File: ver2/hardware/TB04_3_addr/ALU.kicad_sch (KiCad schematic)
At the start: 8 parts, among them J801 Conn_02x05_Odd_Even, J802 Conn_02x05_Odd_Even, J803 Conn_02x05_Odd_Even, J804 Conn_02x05_Odd_Even, J805 Conn_02x05_Odd_Even, J806 Conn_02x05_Odd_Even, J807 Conn_02x05_Odd_Even, J808 Conn_02x05_Odd_Even

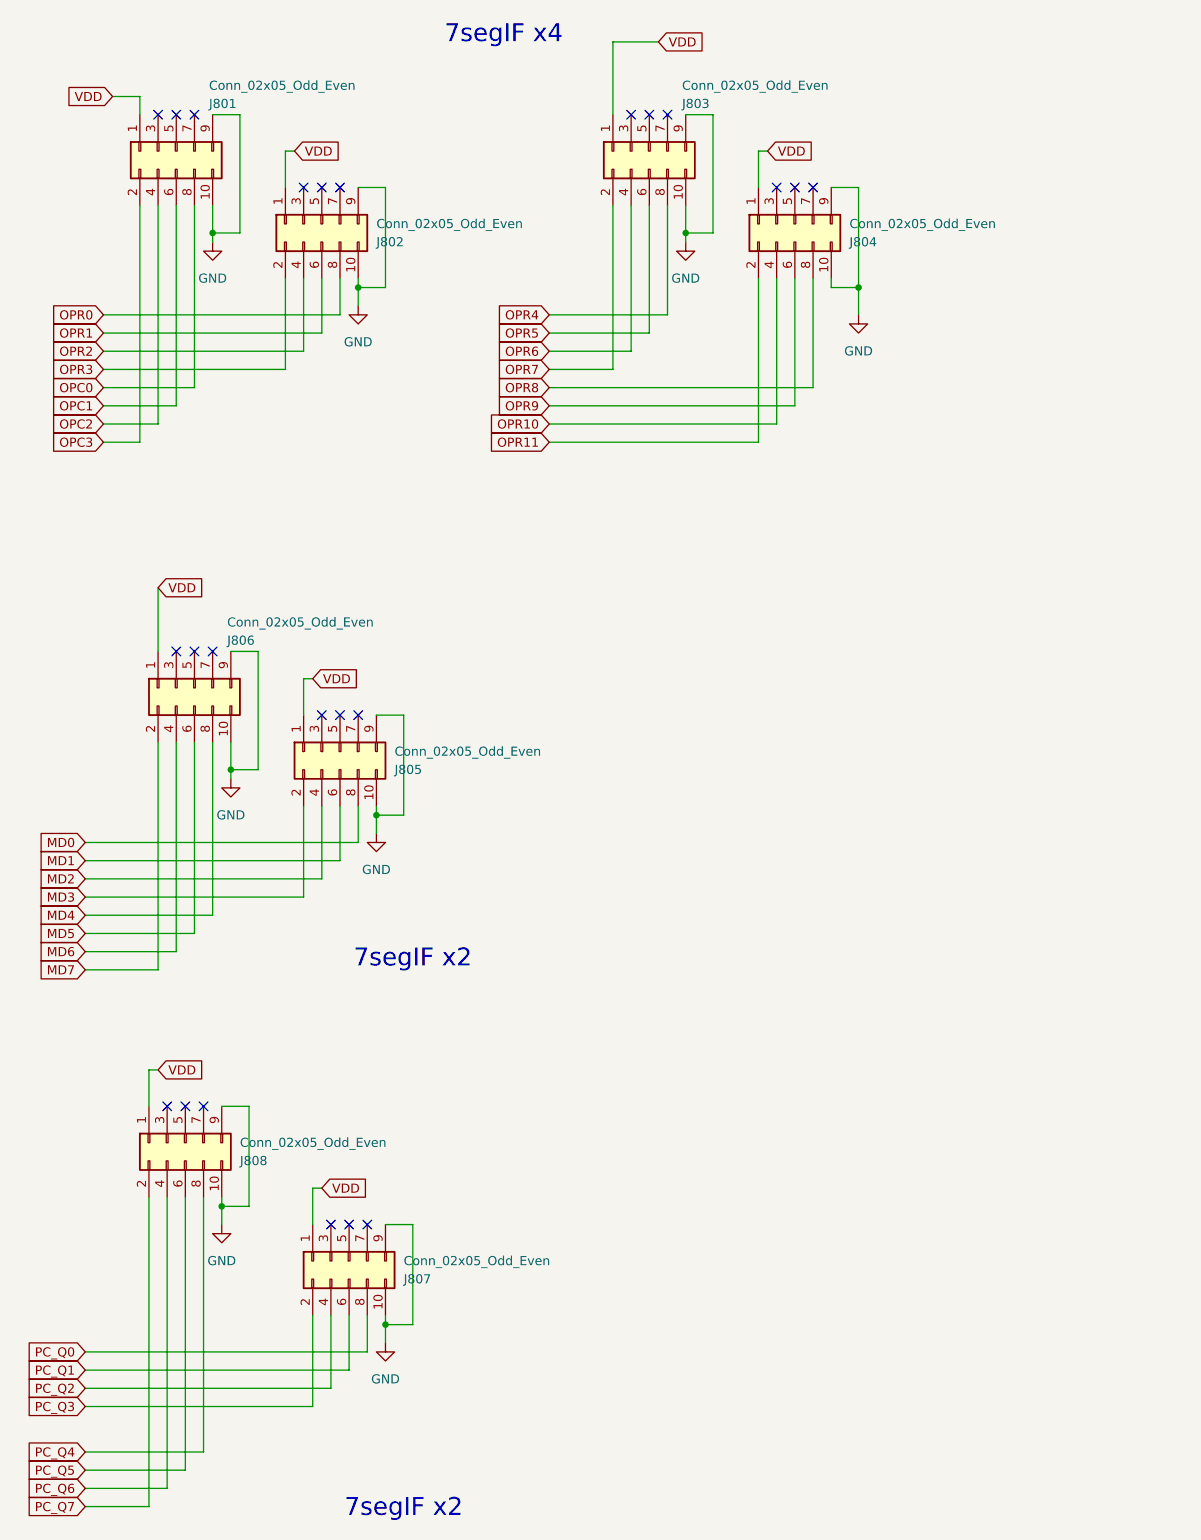
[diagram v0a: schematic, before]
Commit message: ver2: アドレス基板を分割し4枚すべて完了(要修正1件)
TB04_3_addr を分割。45部品・56信号すべてバスへ引き出し済み。
署名が変わったのは J101 のみ(USB-C→バスヘッダ)。
旧トップシート TB04addr8bit.kicad_sch も削除。

要修正: 3_addr の J103 で INPUT/OUTPUT のビット順が 4_io と逆
(pin25=INPUT0 になっている。正は pin25=INPUT3)

Co-Authored-By: Claude Opus 5 <noreply@anthropic.com>
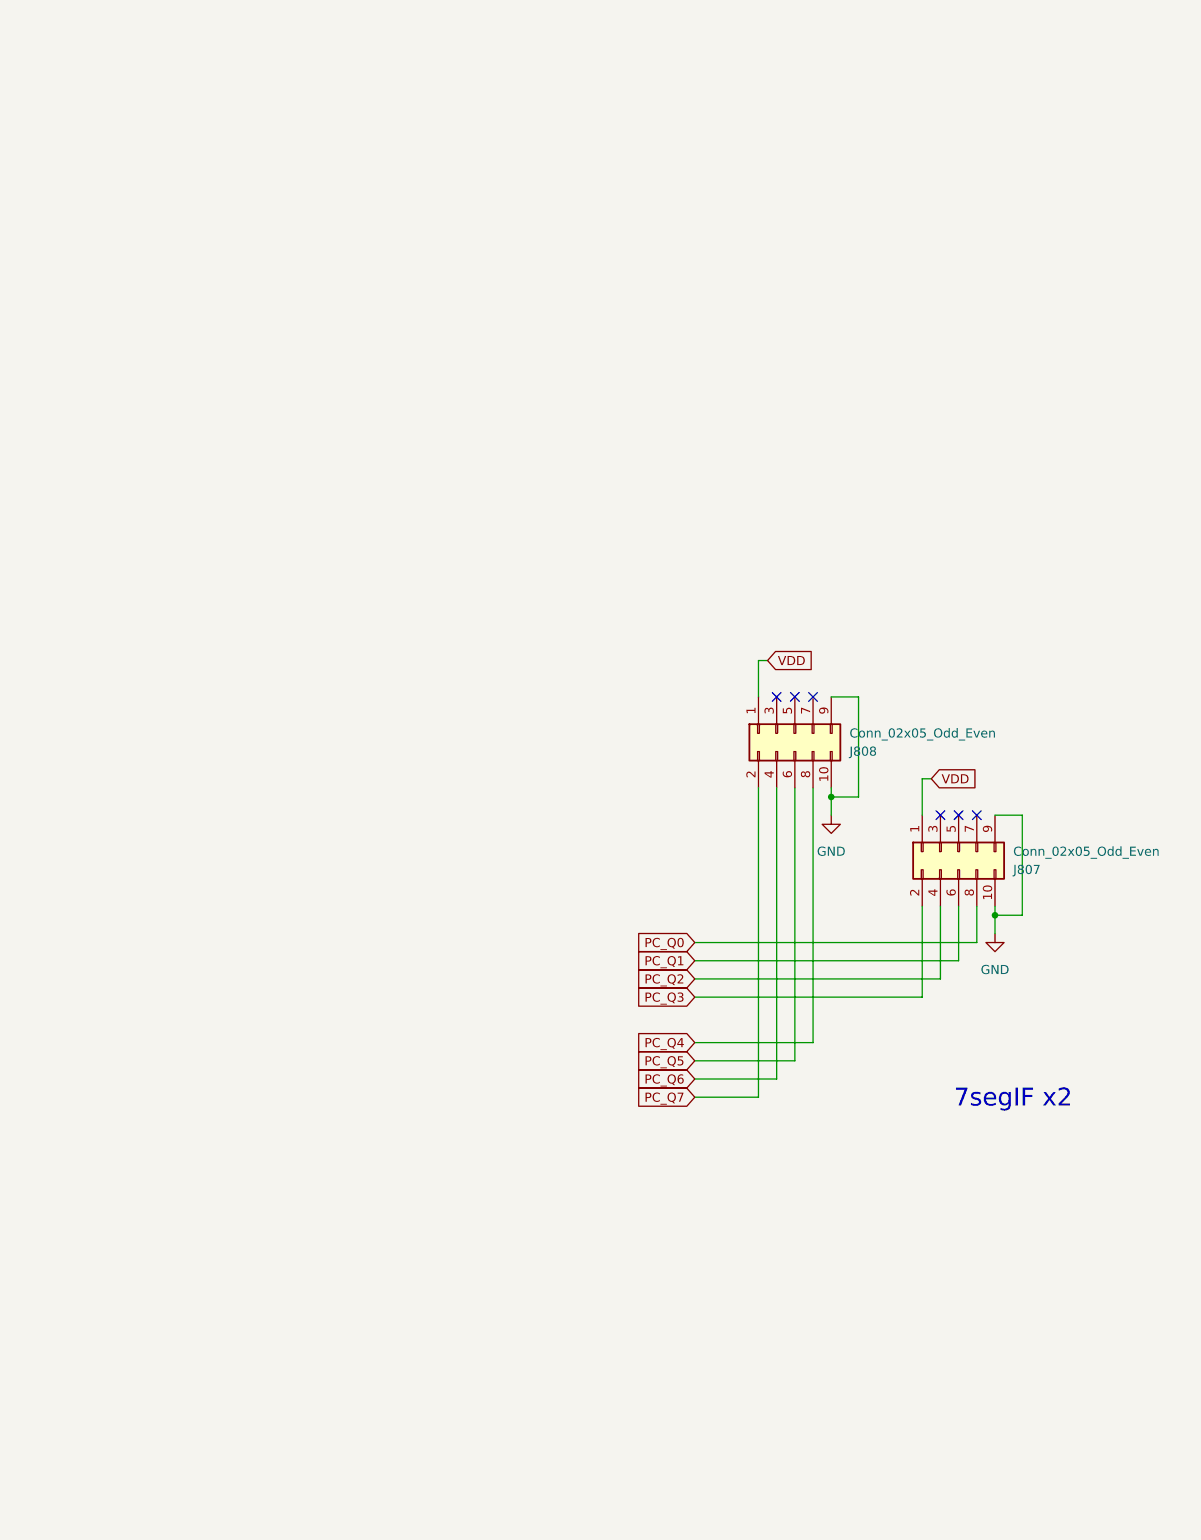
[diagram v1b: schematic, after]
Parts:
- removed J801, J802, J803, J804, J805, J806: Conn_02x05_Odd_Even, symbol Connector_Generic:Conn_02x05_Odd_Even
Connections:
- no-connect marks 24 -> 6
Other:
- note removed: "7segIF x4"
- moved on the sheet: J807, J808
